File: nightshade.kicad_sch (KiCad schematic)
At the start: 95 parts, among them J1 Bus_ISA_16bit, J2 DE15_Plug_HighDensity_Mountin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, J3 Conn_02x13_Odd_Even, Q1 MMBT3904, U1 GD542x_ISA, U10 74HCT244, U11 SOJ_256Kx16, U12 SOJ_256Kx16, U2 SOJ_256Kx16, U3 SOJ_256Kx16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

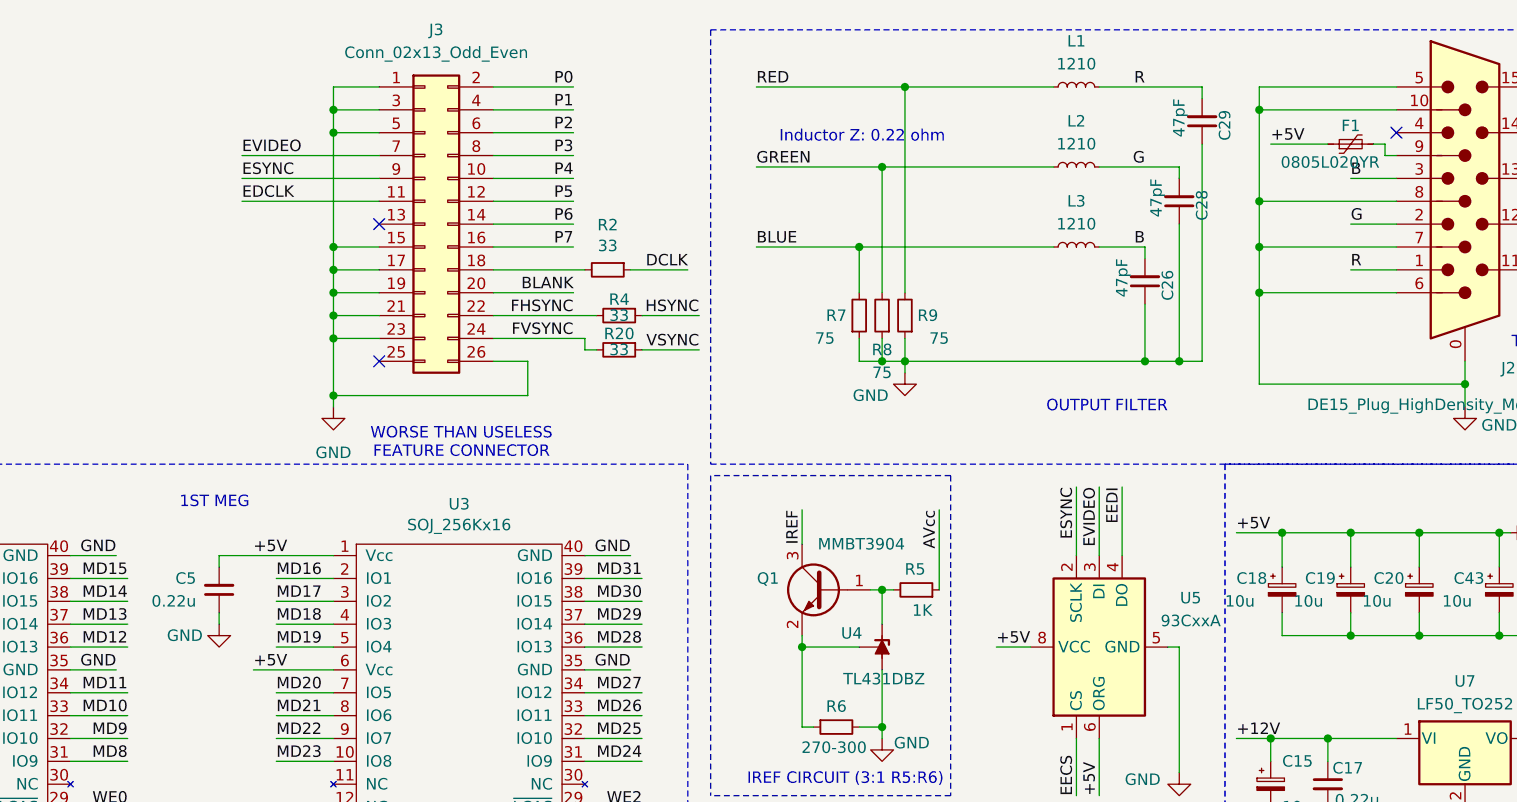
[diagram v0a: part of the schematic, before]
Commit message: Add files via upload
A big bunch of little bug fixes, and combined a capacitor and DIP-28 socket to fix an issue where a ceramic cap was placed too close to the edge connector (mechanical stress issue).
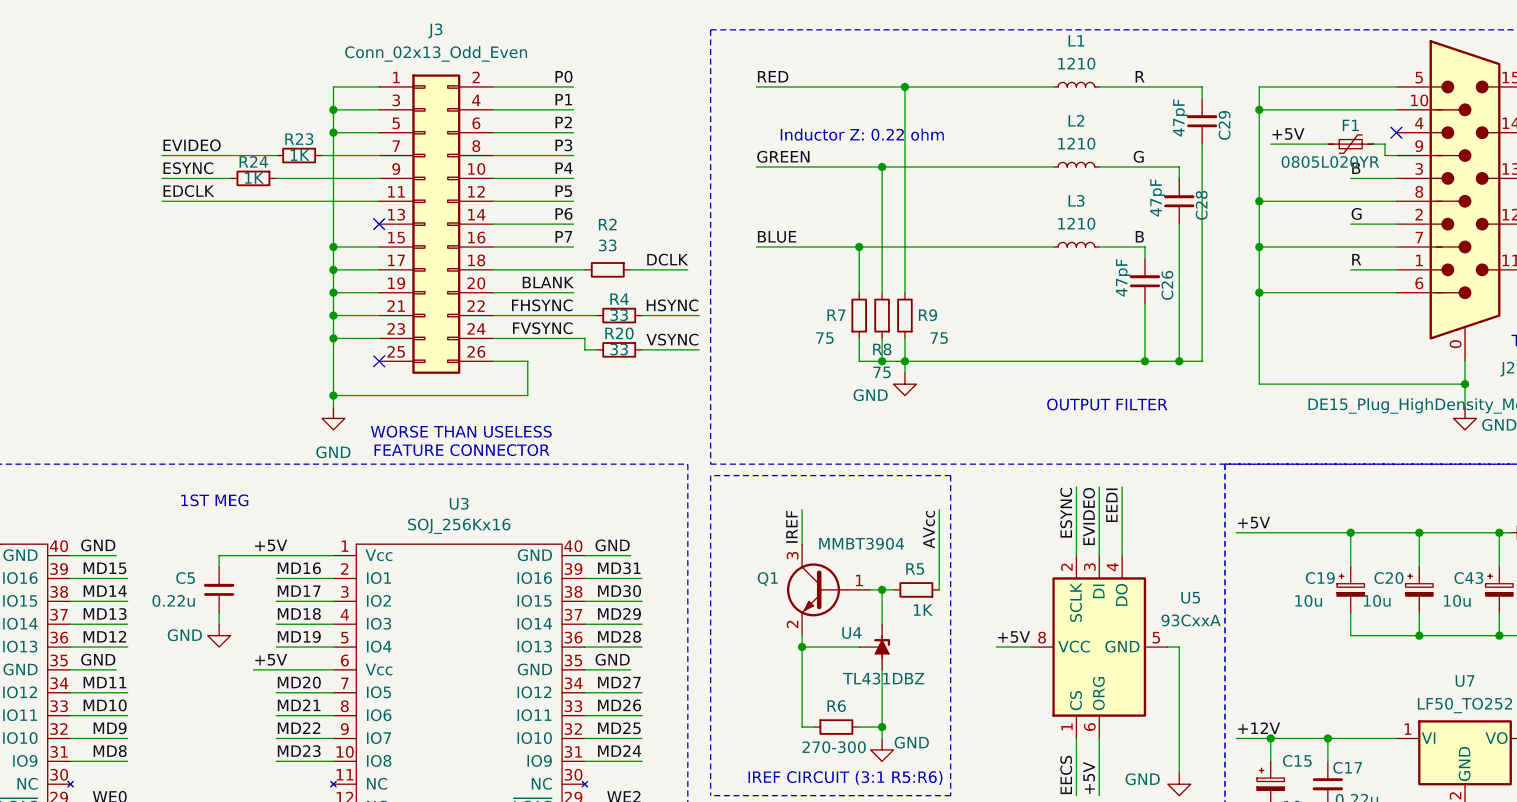
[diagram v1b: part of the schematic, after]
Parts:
- removed C18: 10u, Capacitor_SMD:C_1206_3216Metric, symbol Device:C_Polarized_Small
- added R23, R24: 1K, Resistor_SMD:R_0603_1608Metric, symbol Device:R_Small
- U9: footprint Package_DIP:DIP-28_W15.24mm_Socket -> PDVGA:DIP-28_W15.24mm_Plus_Cap_Socket
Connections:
- net ESYNC: now also R24.2; no longer J3.9 (Pin_9)
- net EVIDEO: now also R23.2; no longer J3.7 (Pin_7)
- new net: J3.7 (Pin_7), R23.1
- new net: J3.9 (Pin_9), R24.1

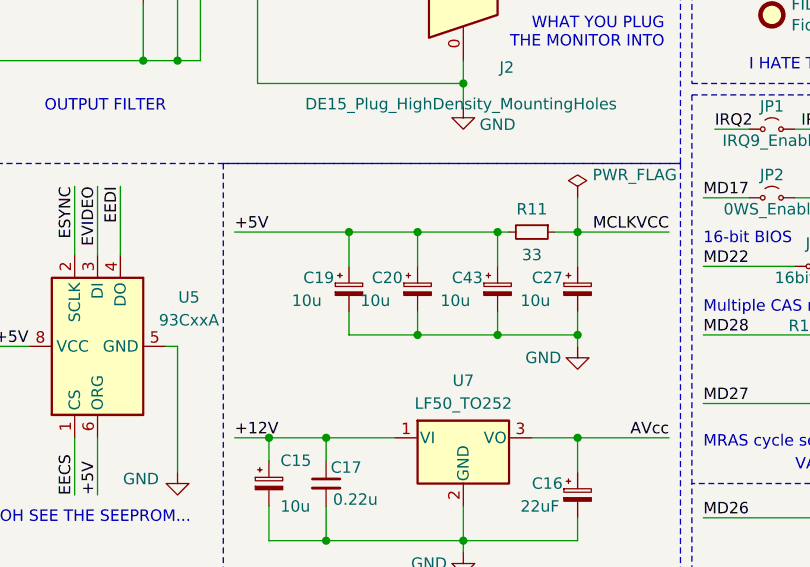
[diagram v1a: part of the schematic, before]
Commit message: Add files via upload
Changed combined footprint back to discrete individual cap and socket. Moved capacitor out from underneath the socket footprint. There, automated assembly should be able to install everything now.
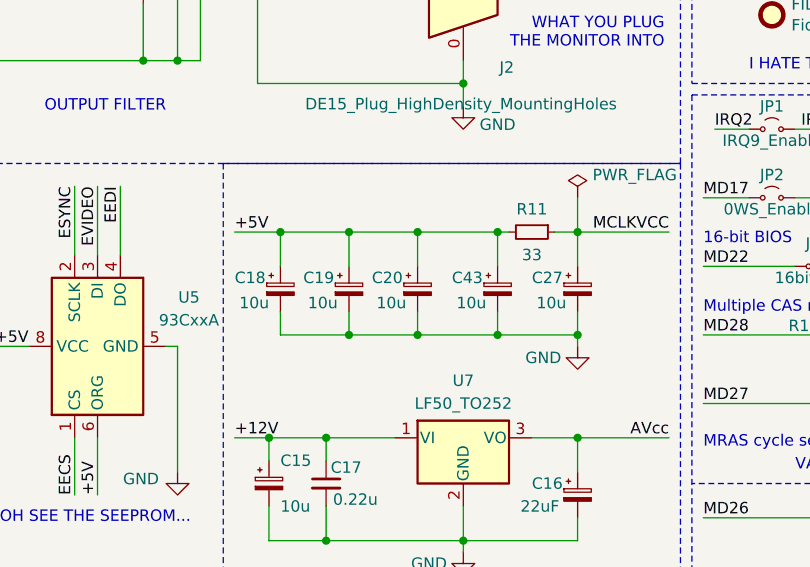
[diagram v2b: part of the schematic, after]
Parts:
- added C18: 10u, Capacitor_SMD:C_1206_3216Metric, symbol Device:C_Polarized_Small
- U9: footprint PDVGA:DIP-28_W15.24mm_Plus_Cap_Socket -> Package_DIP:DIP-28_W15.24mm_Socket
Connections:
- net +5V: now also C18.1
- net GND: now also C18.2
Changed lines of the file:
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@@
 	)
 	(junction
+		(at 330.2 81.28)
+		(diameter 0)
+		(color 0 0 0 0)
+	)
+	(junction
 		(at 166.37 274.32)
 		(diameter 0)
@@
 	)
 	(junction
+		(at 322.58 69.85)
+		(diameter 0)
+		(color 0 0 0 0)
+	)
+	(junction
 		(at 387.35 142.24)
 		(diameter 0)
@@
 	(wire
 		(pts
+			(xy 330.2 81.28) (xy 322.58 81.28)
+		)
+		(stroke
+			(width 0)
+			(type default)
+		)
+	)
+	(wire
+		(pts
 			(xy 370.84 147.32) (xy 374.65 147.32)
 		)
@@
 	(wire
 		(pts
-			(xy 317.5 69.85) (xy 330.2 69.85)
+			(xy 317.5 69.85) (xy 322.58 69.85)
 		)
 		(stroke
@@
 	(wire
 		(pts
+			(xy 322.58 69.85) (xy 322.58 73.66)
+		)
+		(stroke
+			(width 0)
+			(type default)
+		)
+	)
+	(wire
+		(pts
 			(xy 234.95 38.1) (xy 243.84 38.1)
 		)
@@
 	(wire
 		(pts
+			(xy 322.58 81.28) (xy 322.58 78.74)
+		)
+		(stroke
+			(width 0)
+			(type default)
+		)
+	)
+	(wire
+		(pts
 			(xy 297.18 260.35) (xy 288.29 260.35)
 		)
@@
 	(wire
 		(pts
+			(xy 322.58 69.85) (xy 330.2 69.85)
+		)
+		(stroke
+			(width 0)
+			(type default)
+		)
+	)
+	(wire
+		(pts
 			(xy 300.99 207.01) (xy 304.8 207.01)
 		)
@@
 		)
 		(property "Value" "10u"
-			(at 323.85 77.47 0)
+			(at 325.628 77.724 0)
 			(effects
 				(font
@@
 		)
 		(property "Value" "10u"
-			(at 349.25 77.47 0)
+			(at 351.028 77.724 0)
 			(effects
 				(font
@@
 		)
 		(property "Value" "10u"
-			(at 331.47 77.47 0)
+			(at 333.248 77.724 0)
 			(effects
 				(font
@@
 	)
 	(symbol
+		(lib_id "Device:C_Polarized_Small")
+		(at 322.58 76.2 0)
+		(unit 1)
+		(exclude_from_sim no)
+		(in_bom yes)
+		(on_board yes)
+		(dnp no)
+		(property "Reference" "C18"
+			(at 317.5 74.93 0)
+			(effects
+				(font
+					(size 1.27 1.27)
+				)
+				(justify left)
+			)
+		)
+		(property "Value" "10u"
+			(at 318.008 77.724 0)
+			(effects
+				(font
+					(size 1.27 1.27)
+				)
+				(justify left)
+			)
+		)
+		(property "Footprint" "Capacitor_SMD:C_1206_3216Metric"
+			(at 322.58 76.2 0)
+			(effects
+				(font
+					(size 1.27 1.27)
+				)
+				(hide yes)
+			)
+		)
+		(property "Datasheet" "~"
+			(at 322.58 76.2 0)
+			(effects
+				(font
+					(size 1.27 1.27)
+				)
+				(hide yes)
+			)
+		)
+		(property "Description" "Polarized capacitor, small symbol"
+			(at 322.58 76.2 0)
+			(effects
+				(font
+					(size 1.27 1.27)
+				)
+				(hide yes)
+			)
+		)
+		(property "Sim.Device" ""
+			(at 322.58 76.2 0)
+			(effects
+				(font
+					(size 1.27 1.27)
+				)
+				(hide yes)
+			)
+		)
+		(property "Sim.Pins" ""
+			(at 322.58 76.2 0)
+			(effects
+				(font
+					(size 1.27 1.27)
+				)
+				(hide yes)
+			)
+		)
+		(pin "1"
+		)
+		(pin "2"
+		)
+		(instances
+			(project "nightshade"
+				(path "/943ffdfb-b8f3-4ebd-9829-381f0bff885b"
+					(reference "C18")
+					(unit 1)
+				)
+			)
+		)
+	)
+	(symbol
 		(lib_id "74xx:74HCT244")
 		(at 347.98 212.09 0)
@@
 		)
 		(property "Value" "10u"
-			(at 340.36 77.47 0)
+			(at 342.138 77.724 0)
 			(effects
 				(font
@@
 			)
 		)
-		(property "Footprint" "PDVGA:DIP-28_W15.24mm_Plus_Cap_Socket"
+		(property "Footprint" "Package_DIP:DIP-28_W15.24mm_Socket"
 			(at 314.96 157.48 0)
 			(effects

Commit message: Add files via upload
Cheaper parts that do not affect function! Yay!
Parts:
- C1, C10, C17, C2, C21, C22, C24, C25, C3, C32, C33, C34, C35, C36, C37, C38, C39, C4, C40, C42, C44, C5, C6, C9: value 0.22u -> 0.1u
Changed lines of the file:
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@@
 			)
 		)
-		(property "Value" "0.22u"
+		(property "Value" "0.1u"
 			(at 210.82 266.7 90)
 			(effects
@@
 			)
 		)
-		(property "Value" "0.22u"
+		(property "Value" "0.1u"
 			(at 328.422 99.568 0)
 			(effects
@@
 			)
 		)
-		(property "Value" "0.22u"
+		(property "Value" "0.1u"
 			(at 210.82 256.54 90)
 			(effects
@@
 			)
 		)
-		(property "Value" "0.22u"
+		(property "Value" "0.1u"
 			(at 386.08 186.69 0)
 			(effects
@@
 			)
 		)
-		(property "Value" "0.22u"
+		(property "Value" "0.1u"
 			(at 389.89 203.2 0)
 			(effects
@@
 			)
 		)
-		(property "Value" "0.22u"
+		(property "Value" "0.1u"
 			(at 389.89 129.54 90)
 			(effects
@@
 			)
 		)
-		(property "Value" "0.22u"
+		(property "Value" "0.1u"
 			(at 393.7 134.62 90)
 			(effects
@@
 			)
 		)
-		(property "Value" "0.22u"
+		(property "Value" "0.1u"
 			(at 389.89 139.7 90)
 			(effects
@@
 			)
 		)
-		(property "Value" "0.22u"
+		(property "Value" "0.1u"
 			(at 389.89 149.86 90)
 			(effects
@@
 			)
 		)
-		(property "Value" "0.22u"
+		(property "Value" "0.1u"
 			(at 393.7 154.94 90)
 			(effects
@@
 			)
 		)
-		(property "Value" "0.22u"
+		(property "Value" "0.1u"
 			(at 374.65 134.62 90)
 			(effects
@@
 			)
 		)
-		(property "Value" "0.22u"
+		(property "Value" "0.1u"
 			(at 144.78 77.47 0)
 			(effects
@@
 			)
 		)
-		(property "Value" "0.22u"
+		(property "Value" "0.1u"
 			(at 143.51 118.11 0)
 			(effects
@@
 			)
 		)
-		(property "Value" "0.22u"
+		(property "Value" "0.1u"
 			(at 201.93 77.47 0)
 			(effects
@@
 			)
 		)
-		(property "Value" "0.22u"
+		(property "Value" "0.1u"
 			(at 200.66 118.11 0)
 			(effects
@@
 			)
 		)
-		(property "Value" "0.22u"
+		(property "Value" "0.1u"
 			(at 374.65 127 90)
 			(effects
@@
 			)
 		)
-		(property "Value" "0.22u"
+		(property "Value" "0.1u"
 			(at 85.09 119.38 0)
 			(effects
@@
 			)
 		)
-		(property "Value" "0.22u"
+		(property "Value" "0.1u"
 			(at 374.65 149.86 90)
 			(effects
@@
 			)
 		)
-		(property "Value" "0.22u"
+		(property "Value" "0.1u"
 			(at 374.65 157.48 90)
 			(effects
@@
 			)
 		)
-		(property "Value" "0.22u"
+		(property "Value" "0.1u"
 			(at 26.67 78.74 0)
 			(effects
@@
 			)
 		)
-		(property "Value" "0.22u"
+		(property "Value" "0.1u"
 			(at 86.36 78.74 0)
 			(effects
@@
 			)
 		)
-		(property "Value" "0.22u"
+		(property "Value" "0.1u"
 			(at 391.16 177.8 0)
 			(effects
@@
 			)
 		)
-		(property "Value" "0.22u"
+		(property "Value" "0.1u"
 			(at 374.65 142.24 90)
 			(effects
@@
 			)
 		)
-		(property "Value" "0.22u"
+		(property "Value" "0.1u"
 			(at 25.4 119.38 0)
 			(effects
